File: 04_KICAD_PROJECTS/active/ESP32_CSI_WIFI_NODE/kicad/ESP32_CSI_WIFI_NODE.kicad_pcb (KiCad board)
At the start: 2 copper layers, 60 x 95 mm, 43 parts, among them J1 JACK_5V, J2 USB-C_NEEDS_REVIEW, Q1 AO3401A_REV, SW1 BOOT_GPIO0_REVIEW, SW2 RESET_EN_REVIEW, U1 AP63203_NEEDS_REVIEW, U2 ESP32-S3-WROOM-1U, U3 USB_ESD_REV

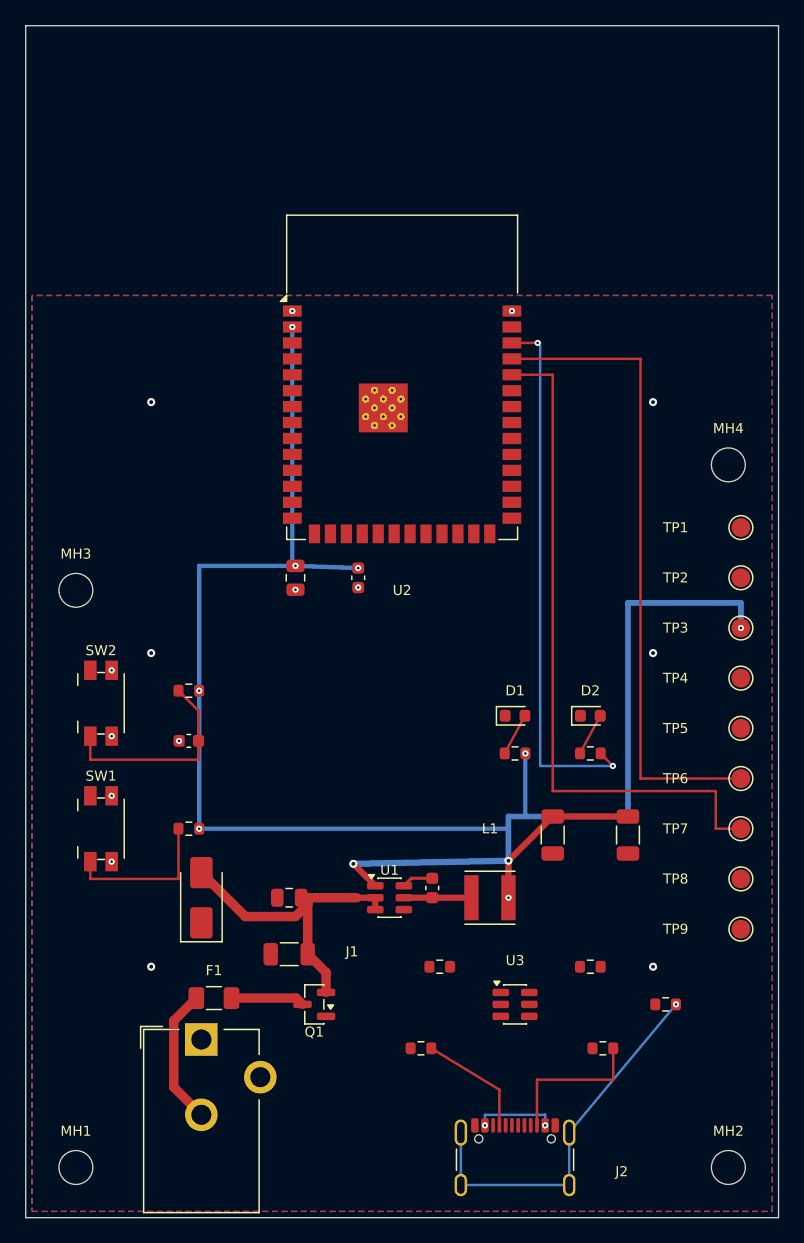
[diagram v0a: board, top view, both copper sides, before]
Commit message: Repair ESP32 CSI WiFi node PCB routing
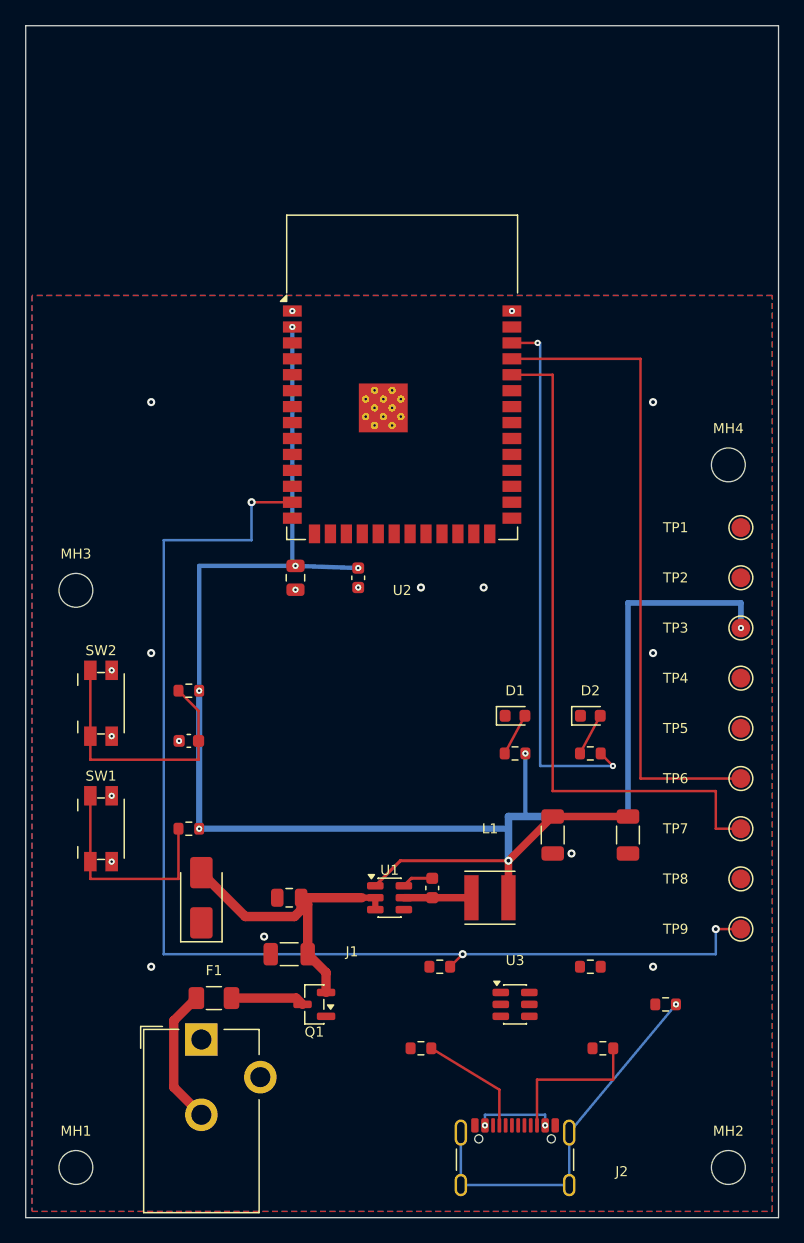
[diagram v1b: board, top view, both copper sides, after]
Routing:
- net /DM_E: track 0.00 -> 95.7 mm, vias 0 -> 3
- net +3V3: track 158.5 -> 151.2 mm, vias 10 -> 8
- net /ESP_EN: track 16.7 -> 21.9 mm
- net /BOOT0: track 12.4 -> 17.6 mm
- net /+5V_PROTECTED: track 24.8 -> 25.8 mm
- net GND: vias 15 -> 19
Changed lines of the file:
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@@
+	)
+	(segment
+		(start 27.863 68.55)
+		(end 29.863 66.55)
+		(width 0.25)
+		(layer "F.Cu")
+		(net 1)
 	)
 	(segment
 		(start 38.475 66.55)
 		(end 42 63.025)
-		(width 0.5)
-		(layer "F.Cu")
-		(net 1)
-	)
-	(segment
-		(start 27.863 68.55)
-		(end 26.113 66.8)
-		(width 0.5)
-		(layer "F.Cu")
-		(net 1)
-	)
-	(segment
-		(start 38.475 66.55)
-		(end 38.475 69.5)
-		(width 0.5)
+		(width 0.6)
+		(layer "F.Cu")
+		(net 1)
+	)
+	(segment
+		(start 38.475 69.5)
+		(end 38.475 66.55)
+		(width 0.6)
 		(layer "F.Cu")
 		(net 1)
@@
 		(start 42 63.025)
 		(end 48 63.025)
-		(width 0.5)
+		(width 0.6)
+		(layer "F.Cu")
+		(net 1)
+	)
+	(segment
+		(start 29.863 66.55)
+		(end 38.475 66.55)
+		(width 0.25)
 		(layer "F.Cu")
 		(net 1)
@@
 	(via
 		(at 13.825 53)
-		(size 0.5)
-		(drill 0.2)
-		(layers "F.Cu" "B.Cu")
-		(net 1)
-	)
-	(via
-		(at 26.113 66.8)
-		(size 0.65)
-		(drill 0.3)
-		(layers "F.Cu" "B.Cu")
-		(net 1)
-	)
-	(via
-		(at 38.475 69.5)
 		(size 0.5)
 		(drill 0.2)
@@
 	)
 	(segment
-		(start 26.113 66.8)
-		(end 38.475 66.55)
-		(width 0.5)
+		(start 38.475 66.55)
+		(end 38.475 63.025)
+		(width 0.6)
 		(layer "B.Cu")
 		(net 1)
@@
 	)
 	(segment
-		(start 13.825 53)
-		(end 13.825 64)
-		(width 0.35)
+		(start 13.825 64)
+		(end 38.475 64)
+		(width 0.5)
 		(layer "B.Cu")
 		(net 1)
@@
 	)
 	(segment
-		(start 38.475 69.5)
-		(end 38.475 63.025)
-		(width 0.45)
-		(layer "B.Cu")
-		(net 1)
-	)
-	(segment
-		(start 38.475 64)
-		(end 38.475 63.025)
-		(width 0.35)
-		(layer "B.Cu")
-		(net 1)
-	)
-	(segment
 		(start 38.475 63.025)
 		(end 42 63.025)
-		(width 0.45)
-		(layer "B.Cu")
-		(net 1)
-	)
-	(segment
-		(start 13.825 64)
-		(end 38.475 64)
-		(width 0.35)
+		(width 0.6)
 		(layer "B.Cu")
 		(net 1)
@@
 	)
 	(segment
+		(start 13.825 53)
+		(end 13.825 64)
+		(width 0.5)
+		(layer "B.Cu")
+		(net 1)
+	)
+	(segment
 		(start 39.825 58)
 		(end 39.825 63.025)
@@
 	)
 	(segment
-		(start 21.5 71)
+		(start 21.95 69.5)
 		(end 22.475 70.025)
 		(width 0.75)
@@
 	)
 	(segment
-		(start 22.475 70.025)
-		(end 22.475 69.5)
+		(start 17.5 71)
+		(end 21.425 71)
+		(width 0.75)
+		(layer "F.Cu")
+		(net 4)
+	)
+	(segment
+		(start 14 67.5)
+		(end 17.5 71)
 		(width 0.75)
 		(layer "F.Cu")
@@
 	)
 	(segment
-		(start 17.5 71)
-		(end 21.5 71)
-		(width 0.75)
-		(layer "F.Cu")
-		(net 4)
-	)
-	(segment
-		(start 22.475 74)
-		(end 23.938 75.463)
-		(width 0.75)
-		(layer "F.Cu")
-		(net 4)
-	)
-	(segment
-		(start 14 67.5)
-		(end 17.5 71)
+		(start 22.475 70.025)
+		(end 22.475 74)
 		(width 0.75)
 		(layer "F.Cu")
@@
 	)
 	(segment
-		(start 22.475 69.5)
-		(end 26.4 69.5)
-		(width 0.75)
-		(layer "F.Cu")
-		(net 4)
-	)
-	(segment
-		(start 22.475 70.025)
-		(end 22.475 74)
-		(width 0.75)
-		(layer "F.Cu")
-		(net 4)
-	)
-	(segment
-		(start 26.4 69.5)
+		(start 21.425 71)
+		(end 21.95 70.475)
+		(width 0.75)
+		(layer "F.Cu")
+		(net 4)
+	)
+	(segment
+		(start 26.8 69.5)
 		(end 27.863 69.5)
 		(width 0.5)
@@
 	)
 	(segment
+		(start 21.95 69.5)
+		(end 26.8 69.5)
+		(width 0.75)
+		(layer "F.Cu")
+		(net 4)
+	)
+	(segment
+		(start 22.475 74)
+		(end 23.938 75.463)
+		(width 0.75)
+		(layer "F.Cu")
+		(net 4)
+	)
+	(segment
+		(start 21.95 70.475)
+		(end 21.95 69.5)
+		(width 0.75)
+		(layer "F.Cu")
+		(net 4)
+	)
+	(segment
 		(start 12.175 64)
 		(end 12.175 68)
@@
 		(start 5.15 68)
 		(end 5.15 66.625)
+		(width 0.2)
+		(layer "F.Cu")
+		(net 5)
+	)
+	(segment
+		(start 5.15 66.625)
+		(end 5.15 61.375)
 		(width 0.2)
 		(layer "F.Cu")
@@
 		(start 32.4 69.5)
 		(end 35.525 69.5)
-		(width 0.5)
+		(width 0.6)
 		(layer "F.Cu")
 		(net 7)
@@
 		(start 30.137 69.5)
 		(end 32.4 69.5)
-		(width 0.5)
+		(width 0.6)
 		(layer "F.Cu")
 		(net 7)
@@
 	)
 	(segment
+		(start 34.825 74)
+		(end 33.825 75)
+		(width 0.2)
+		(layer "F.Cu")
+		(net 11)
+	)
+	(segment
+		(start 55 72)
+		(end 57 72)
+		(width 0.2)
+		(layer "F.Cu")
+		(net 11)
+	)
+	(segment
+		(start 21.25 37.98)
+		(end 18 37.98)
+		(width 0.2)
+		(layer "F.Cu")
+		(net 11)
+	)
+	(via
+		(at 55 72)
+		(size 0.65)
+		(drill 0.3)
+		(layers "F.Cu" "B.Cu")
+		(net 11)
+	)
+	(via
+		(at 18 37.98)
+		(size 0.65)
+		(drill 0.3)
+		(layers "F.Cu" "B.Cu")
+		(net 11)
+	)
+	(via
+		(at 34.825 74)
+		(size 0.65)
+		(drill 0.3)
+		(layers "F.Cu" "B.Cu")
+		(net 11)
+	)
+	(segment
+		(start 18 41)
+		(end 11 41)
+		(width 0.2)
+		(layer "B.Cu")
+		(net 11)
+	)
+	(segment
+		(start 18 37.98)
+		(end 18 41)
+		(width 0.2)
+		(layer "B.Cu")
+		(net 11)
+	)
+	(segment
+		(start 11 41)
+		(end 11 74)
+		(width 0.2)
+		(layer "B.Cu")
+		(net 11)
+	)
+	(segment
+		(start 11 74)
+		(end 34.825 74)
+		(width 0.2)
+		(layer "B.Cu")
+		(net 11)
+	)
+	(segment
+		(start 55 74)
+		(end 55 72)
+		(width 0.2)
+		(layer "B.Cu")
+		(net 11)
+	)
+	(segment
+		(start 34.825 74)
+		(end 55 74)
+		(width 0.2)
+		(layer "B.Cu")
+		(net 11)
+	)
+	(segment
 		(start 13.775 58.5)
 		(end 5.15 58.5)
@@
 	)
 	(segment
+		(start 5.15 56.625)
+		(end 5.15 51.375)
+		(width 0.2)
+		(layer "F.Cu")
+		(net 14)
+	)
+	(segment
 		(start 38.175 58)
 		(end 39.788 55)
@@
 	)
 	(via
+		(at 31.5 44.775)
+		(size 0.65)
+		(drill 0.3)
+		(layers "F.Cu" "B.Cu")
+		(net 21)
+	)
+	(via
+		(at 36.5 44.775)
+		(size 0.65)
+		(drill 0.3)
+		(layers "F.Cu" "B.Cu")
+		(net 21)
+	)
+	(via
 		(at 10 50)
 		(size 0.65)
 		(drill 0.3)
+		(layers "F.Cu" "B.Cu")
+		(net 21)
+	)
+	(via
+		(at 43.5 65.974999)
+		(size 0.65)
+		(drill 0.3)
+		(layers "F.Cu" "B.Cu")
+		(net 21)
+	)
+	(via
+		(at 19 72.6)
+		(size 0.65)
+		(drill 0.3)
